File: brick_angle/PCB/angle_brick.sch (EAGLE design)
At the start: 2 parts, among them J1 3PIN, U1 ANGLE

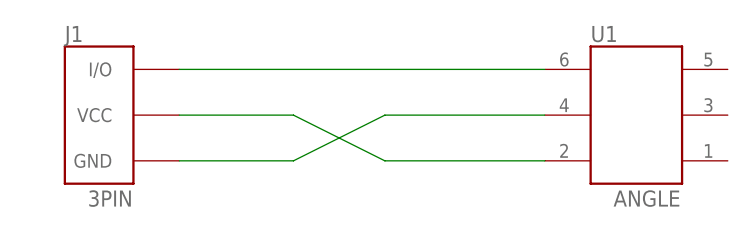
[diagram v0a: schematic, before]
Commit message: brick_angle:  (PCB)refine board
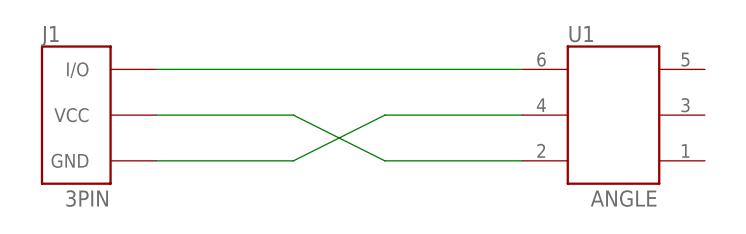
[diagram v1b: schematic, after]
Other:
- moved on the sheet: J1, U1
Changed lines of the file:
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@@
 <instances>
 <instance part="U$2" gate="G$1" x="0" y="0"/>
-<instance part="J1" gate="G$1" x="96.52" y="88.9" smashed="yes">
-<attribute name="NAME" x="91.44" y="97.028" size="1.778" layer="95"/>
-<attribute name="VALUE" x="93.98" y="78.74" size="1.778" layer="96"/>
+<instance part="J1" gate="G$1" x="93.98" y="88.9" smashed="yes">
+<attribute name="NAME" x="88.9" y="97.028" size="1.778" layer="95"/>
+<attribute name="VALUE" x="91.44" y="78.74" size="1.778" layer="96"/>
 </instance>
-<instance part="U1" gate="G$1" x="154.94" y="88.9" smashed="yes" rot="R180">
-<attribute name="NAME" x="149.86" y="97.028" size="1.778" layer="95"/>
-<attribute name="VALUE" x="152.4" y="78.74" size="1.778" layer="96"/>
+<instance part="U1" gate="G$1" x="152.4" y="88.9" smashed="yes" rot="R180">
+<attribute name="NAME" x="147.32" y="97.028" size="1.778" layer="95"/>
+<attribute name="VALUE" x="149.86" y="78.74" size="1.778" layer="96"/>
 </instance>
 </instances>
@@
 <net name="N$2" class="0">
 <segment>
-<wire x1="144.78" y1="83.82" x2="127" y2="83.82" width="0.1524" layer="91"/>
+<wire x1="142.24" y1="83.82" x2="127" y2="83.82" width="0.1524" layer="91"/>
 <wire x1="127" y1="83.82" x2="116.84" y2="88.9" width="0.1524" layer="91"/>
-<wire x1="116.84" y1="88.9" x2="104.14" y2="88.9" width="0.1524" layer="91"/>
+<wire x1="116.84" y1="88.9" x2="101.6" y2="88.9" width="0.1524" layer="91"/>
 <pinref part="J1" gate="G$1" pin="VCC"/>
 <pinref part="U1" gate="G$1" pin="2"/>
@@
 <net name="N$1" class="0">
 <segment>
-<wire x1="104.14" y1="93.98" x2="144.78" y2="93.98" width="0.1524" layer="91"/>
+<wire x1="101.6" y1="93.98" x2="142.24" y2="93.98" width="0.1524" layer="91"/>
 <pinref part="J1" gate="G$1" pin="I/O"/>
 <pinref part="U1" gate="G$1" pin="6"/>
@@
 <net name="GND" class="0">
 <segment>
-<wire x1="144.78" y1="88.9" x2="127" y2="88.9" width="0.1524" layer="91"/>
+<wire x1="142.24" y1="88.9" x2="127" y2="88.9" width="0.1524" layer="91"/>
 <wire x1="127" y1="88.9" x2="116.84" y2="83.82" width="0.1524" layer="91"/>
-<wire x1="116.84" y1="83.82" x2="104.14" y2="83.82" width="0.1524" layer="91"/>
+<wire x1="116.84" y1="83.82" x2="101.6" y2="83.82" width="0.1524" layer="91"/>
 <pinref part="J1" gate="G$1" pin="GND"/>
 <pinref part="U1" gate="G$1" pin="4"/>

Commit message: refine PCB board fix library
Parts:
- J1: device fabo:BRICK_3PIN -> gclue:BRICK_3PIN
- U1: device fabo:BRICK_ANGLE -> gclue:ROTARYENCORDER_BRICK
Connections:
- net N$2 renamed VCC
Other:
- moved on the sheet: J1, U1
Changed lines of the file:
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@@
 <setting verticaltext="up"/>
 </settings>
-<grid distance="0.1" unitdist="inch" unit="inch" style="lines" multiple="1" display="yes" altdistance="0.01" altunitdist="inch" altunit="inch"/>
+<grid distance="0.1" unitdist="inch" unit="inch" style="lines" multiple="1" display="no" altdistance="0.01" altunitdist="inch" altunit="inch"/>
 <layers>
 <layer number="1" name="Top" color="4" fill="1" visible="no" active="no"/>
@@
 </classes>
 <parts>
-<part name="U$2" library="fabo" deviceset="A4L-LOC" device=""/>
-<part name="J1" library="fabo" deviceset="BRICK_3PIN" device="" value="3PIN"/>
-<part name="U1" library="fabo" deviceset="BRICK_ANGLE" device="" value="ANGLE"/>
+<part name="U$1" library="gclue" deviceset="A4L-LOC" device=""/>
+<part name="J1" library="gclue" deviceset="BRICK_3PIN" device="" value="3PIN"/>
+<part name="U1" library="gclue" deviceset="ROTARYENCORDER_BRICK" device="" value="ANGLE"/>
 </parts>
 <sheets>
@@
 </plain>
 <instances>
-<instance part="U$2" gate="G$1" x="0" y="0"/>
-<instance part="J1" gate="G$1" x="93.98" y="88.9" smashed="yes">
-<attribute name="NAME" x="88.9" y="97.028" size="1.778" layer="95"/>
-<attribute name="VALUE" x="91.44" y="78.74" size="1.778" layer="96"/>
+<instance part="U$1" gate="G$1" x="0" y="0"/>
+<instance part="J1" gate="G$1" x="91.44" y="88.9" smashed="yes">
+<attribute name="NAME" x="86.36" y="97.028" size="1.778" layer="95"/>
 </instance>
-<instance part="U1" gate="G$1" x="152.4" y="88.9" smashed="yes" rot="R180">
-<attribute name="NAME" x="147.32" y="97.028" size="1.778" layer="95"/>
-<attribute name="VALUE" x="149.86" y="78.74" size="1.778" layer="96"/>
+<instance part="U1" gate="G$1" x="154.94" y="88.9" smashed="yes" rot="R180">
+<attribute name="NAME" x="149.86" y="97.028" size="1.778" layer="95"/>
+<attribute name="VALUE" x="152.4" y="78.74" size="1.778" layer="96"/>
 </instance>
 </instances>
@@
 </busses>
 <nets>
-<net name="N$2" class="0">
+<net name="N$1" class="0">
 <segment>
-<wire x1="142.24" y1="83.82" x2="127" y2="83.82" width="0.1524" layer="91"/>
-<wire x1="127" y1="83.82" x2="116.84" y2="88.9" width="0.1524" layer="91"/>
-<wire x1="116.84" y1="88.9" x2="101.6" y2="88.9" width="0.1524" layer="91"/>
-<pinref part="J1" gate="G$1" pin="VCC"/>
-<pinref part="U1" gate="G$1" pin="2"/>
+<pinref part="J1" gate="G$1" pin="I/O"/>
+<pinref part="U1" gate="G$1" pin="6"/>
+<wire x1="99.06" y1="93.98" x2="144.78" y2="93.98" width="0.1524" layer="91"/>
 </segment>
 </net>
-<net name="N$1" class="0">
+<net name="VCC" class="0">
 <segment>
-<wire x1="101.6" y1="93.98" x2="142.24" y2="93.98" width="0.1524" layer="91"/>
-<pinref part="J1" gate="G$1" pin="I/O"/>
-<pinref part="U1" gate="G$1" pin="6"/>
+<pinref part="J1" gate="G$1" pin="VCC"/>
+<wire x1="99.06" y1="88.9" x2="116.84" y2="88.9" width="0.1524" layer="91"/>
+<wire x1="116.84" y1="88.9" x2="127" y2="83.82" width="0.1524" layer="91"/>
+<pinref part="U1" gate="G$1" pin="2"/>
+<wire x1="127" y1="83.82" x2="144.78" y2="83.82" width="0.1524" layer="91"/>
 </segment>
 </net>
 <net name="GND" class="0">
 <segment>
-<wire x1="142.24" y1="88.9" x2="127" y2="88.9" width="0.1524" layer="91"/>
-<wire x1="127" y1="88.9" x2="116.84" y2="83.82" width="0.1524" layer="91"/>
-<wire x1="116.84" y1="83.82" x2="101.6" y2="83.82" width="0.1524" layer="91"/>
 <pinref part="J1" gate="G$1" pin="GND"/>
+<wire x1="99.06" y1="83.82" x2="116.84" y2="83.82" width="0.1524" layer="91"/>
+<wire x1="116.84" y1="83.82" x2="127" y2="88.9" width="0.1524" layer="91"/>
 <pinref part="U1" gate="G$1" pin="4"/>
+<wire x1="127" y1="88.9" x2="144.78" y2="88.9" width="0.1524" layer="91"/>
 </segment>
 </net>
